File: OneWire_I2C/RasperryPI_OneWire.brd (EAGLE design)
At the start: 63.5 x 28.6 mm, 25 parts, among them U1 P82B715D, U2 DS2482-800

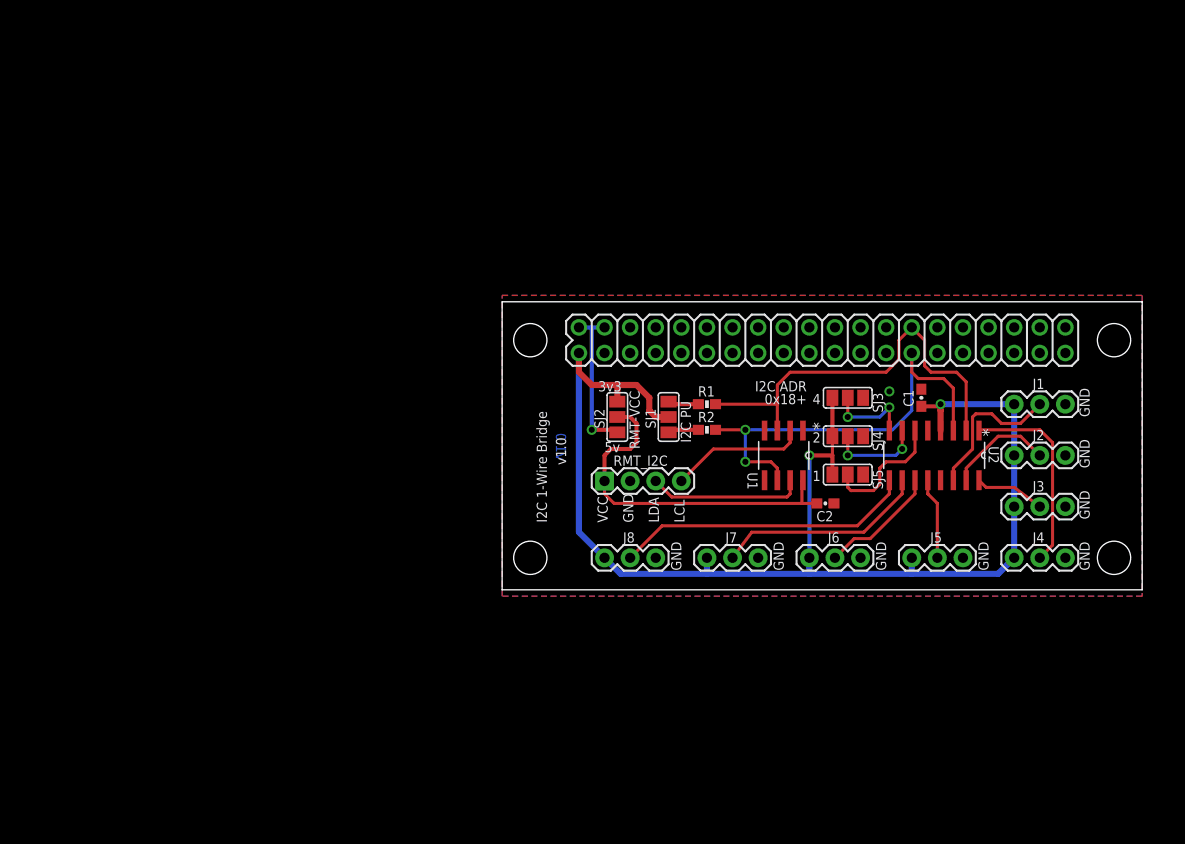
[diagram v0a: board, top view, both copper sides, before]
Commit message: Added Raspberry pi board, updated I2C extender pullup resistors to other boards
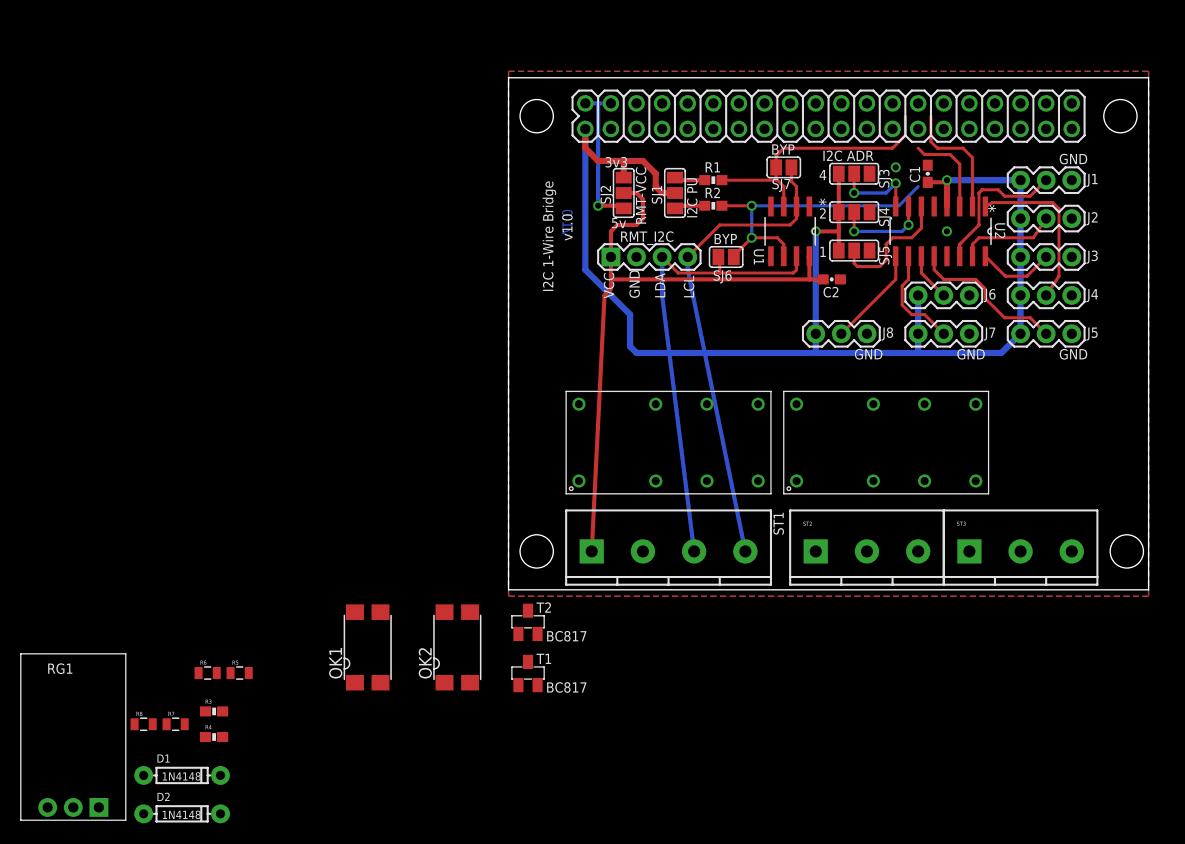
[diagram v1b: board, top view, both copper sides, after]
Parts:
- added D1, D2: 1N4148, SparkFun-DiscreteSemi:DIODE-1N4148
- added OK1, OK2: LTV816S, optocoupler:SMD4
- added R3, R4: (no value), SparkFun-Resistors:0603-RES
- added R5, R6, R7, R8: (no value), SparkFun-Resistors:0805
- added RG1: (no value), Puffin:MURATA_REG_HOR
- added RLY1, RLY2: HK19F_5V_DPDT_RELAY, Puffin:DIP16-RELAY
- added SJ6, SJ7: (no value), jumper:SJ
- added ST1: (no value), Puffin:SCREWTERM_0.2X4
- added ST2, ST3: (no value), Puffin:SCREWTERM_0.2X3
- added T1, T2: BC817, Puffin:SOT-23
- moved J7 30.5 mm to (41.3, 25.4)
- moved J8 30.5 mm to (31.1, 25.4)
- moved J6 28.2 mm to (41.3, 29.2)
- moved J4 26.0 mm to (51.4, 29.2)
- moved J3 24.8 mm to (51.4, 33.0)
- moved J5 24.7 mm to (51.4, 25.4)
- moved J2 23.5 mm to (51.4, 36.8)
- moved C2 22.2 mm to (32.7, 30.8)
- moved J1 22.2 mm to (51.4, 40.6)
- moved PI 22.2 mm to (32.4, 47.0)
- moved R1 22.2 mm to (21.0, 40.6)
- moved R2 22.2 mm to (21.0, 38.1)
- moved RMT_I2C 22.2 mm to (10.8, 33.0)
- moved SJ4 22.2 mm to (34.9, 37.5)
- moved SJ5 22.2 mm to (34.9, 33.7)
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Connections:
- new net 12V: D1.C, D2.C, OK1.4, OK2.4, RG1.1, RLY1.1, RLY2.1
- new net N$12: R4.2, T2.1
- new net N$13: D2.A, RLY2.16, T2.3
- new net N$14: D1.A, RLY1.16, T1.3
- new net N$15: R3.2, T1.1
- new net N$16: OK1.3, R3.1
- new net N$17: RLY2.4, ST3.1
- new net N$18: RLY2.6, ST3.2
- new net N$19: RLY2.8, ST3.3
- new net N$20: RLY1.4, ST2.1
- new net N$21: RLY1.6, ST2.2
- new net N$22: RLY1.8, ST2.3
- new net N$23: OK2.1, R6.1
- new net N$24: OK1.1, R5.1
- new net RLY1: OK1.2, PI.37
- new net RLY2: OK2.2, PI.35
- new net VSEL: C2.1, R7.2, R8.2, RMT_I2C.1, SJ2.2, ST1.1, U1.8
- net 3.3V: now also R5.2, R6.2
- net 5V: now also RG1.3
- net GND: now also PI.14, PI.20, RG1.2, ST1.2, T1.2, T2.2
- net LCL: now also R8.1, SJ7.1, ST1.4
- net LDA: now also R7.1, SJ6.1, ST1.3
- net N$11: now also OK2.3, R4.1; no longer C2.1, RMT_I2C.1, SJ2.2, U1.8
- net SCL: now also PI.5, SJ7.2; no longer PI.28
- net SDA: now also PI.3, SJ6.2; no longer PI.27
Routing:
- net VSEL: track 0.00 -> 64.5 mm
- net N$11: track 35.4 -> 0.00 mm
- net LCL: track 13.6 -> 47.5 mm
- net LDA: track 15.5 -> 46.6 mm
- net N$10: track 29.7 -> 9.93 mm
- net N$7: track 21.0 -> 10.4 mm
- net N$5: track 8.09 -> 15.6 mm
- net N$6: track 11.9 -> 4.81 mm
- net SDA: track 44.7 -> 39.7 mm
- net N$4: track 19.8 -> 16.6 mm
- net SCL: track 41.4 -> 38.6 mm
- net 3.3V: track 130.5 -> 133.2 mm
- net N$2: track 10.6 -> 9.78 mm
- net N$3: track 6.96 -> 7.64 mm
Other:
- board size 63.5 x 28.6 mm -> 63.5 x 50.8 mm
- board text added: "BYP"
- board text removed: "0x18+"

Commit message: Finished RPI 1Wire board
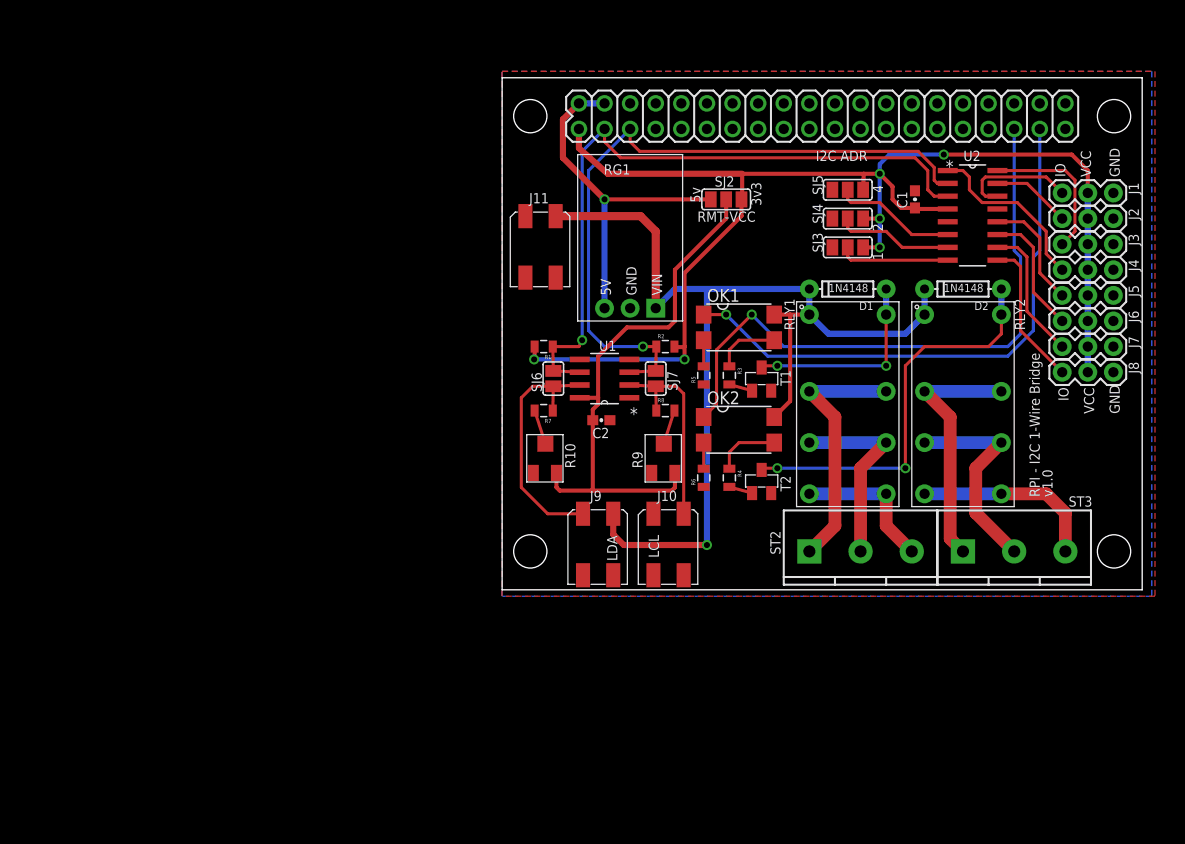
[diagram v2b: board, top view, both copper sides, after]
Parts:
- removed RMT_I2C: (no value), SparkFun-Connectors:1X04
- removed SJ1: (no value), jumper:SJ_2
- removed ST1: (no value), Puffin:SCREWTERM_0.2X4
- added J10, J11, J9: MOLEX_MINILITE_TRAP_2, Puffin:MOLEX_MINILITE_TRAP_2
- added R10, R9: (no value), Puffin:POT_3MM
- R1, R2: value 2.2k -> (none); device SparkFun-Resistors:0603-RES -> SparkFun-Resistors:0805
- R3, R4: device SparkFun-Resistors:0603-RES -> SparkFun-Resistors:0805
- moved D2 93.3 mm to (45.7, 29.8), turned to 180 degrees
- moved D1 81.8 mm to (34.3, 29.8), turned to 180 degrees
- moved RG1 74.2 mm to (12.7, 27.9)
- moved R3 61.0 mm to (22.5, 21.3), turned to 270 degrees
- moved R8 60.4 mm to (16.2, 17.8)
- moved R4 57.2 mm to (22.5, 11.1), turned to 270 degrees
- moved R5 54.7 mm to (20.0, 21.3), turned to 90 degrees
- moved R6 52.9 mm to (20.0, 11.1), turned to 90 degrees
- moved OK1 48.6 mm to (23.5, 26.0), turned to 270 degrees
- moved R7 48.0 mm to (4.13, 17.8), turned to 180 degrees
- moved T1 37.3 mm to (25.7, 21.0)
- moved OK2 35.3 mm to (23.5, 15.9), turned to 270 degrees
- moved T2 27.1 mm to (25.7, 10.8)
- moved C2 26.8 mm to (9.84, 16.8)
- moved J8 24.7 mm to (55.6, 21.6)
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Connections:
- removed net N$8: R2.1, SJ1.1
- removed net N$9: R1.1, SJ1.3
- new net N$25: R10.2, R7.2
- new net N$26: R8.2, R9.2
- net 12V: now also J11.1, J9.1
- net 3.3V: now also J1.2, J2.2, J3.2, J4.2, J5.2, J6.2, J7.2, J8.2, R1.2, R2.2; no longer J1.1, J2.1, J3.1, J4.1, J5.1, J6.1, J7.1, J8.1, R5.2, R6.2, SJ1.2
- net GND: now also J10.2, J11.2, R5.1, R6.1; no longer RMT_I2C.2, ST1.2
- net LCL: now also J10.1; no longer RMT_I2C.4, ST1.4
- net LDA: now also J9.2; no longer RMT_I2C.3, ST1.3
- net N$1: now also J1.1; no longer J1.2
- net N$10: now also J8.1; no longer J8.2
- net N$17: now also RLY2.13
- net N$18: now also RLY2.11
- net N$19: now also RLY2.9
- net N$2: now also J2.1; no longer J2.2
- net N$20: now also RLY1.13
- net N$21: now also RLY1.11
- net N$22: now also RLY1.9
- net N$23: now also OK1.2, R5.2; no longer OK2.1, R6.1
- net N$24: now also OK2.2, R6.2; no longer OK1.1, R5.1
- net N$3: now also J3.1; no longer J3.2
- net N$4: now also J4.1; no longer J4.2
- net N$5: now also J5.1; no longer J5.2
- net N$6: now also J6.1; no longer J6.2
- net N$7: now also J7.1; no longer J7.2
- net RLY1: now also OK1.1; no longer OK1.2
- net RLY2: now also OK2.1; no longer OK2.2
- net SCL: now also R2.1; no longer R1.2
- net SDA: now also R1.1; no longer R2.2
- net VSEL: now also R10.1, R9.1; no longer R7.2, R8.2, RMT_I2C.1, ST1.1
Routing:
- net 12V: track 0.00 -> 103.8 mm, vias 0 -> 1
- net RLY2: track 0.00 -> 61.2 mm, vias 0 -> 1
- net RLY1: track 0.00 -> 55.7 mm, vias 0 -> 1
- net N$13: track 0.00 -> 39.8 mm, vias 0 -> 2
- net SCL: track 38.6 -> 69.4 mm, vias 0 -> 1
- net SDA: track 39.7 -> 68.9 mm, vias 2 -> 1
- net LCL: track 47.5 -> 20.0 mm
- net N$20: track 0.00 -> 25.6 mm
- net N$17: track 0.00 -> 25.1 mm
- net LDA: track 46.6 -> 24.8 mm
- net N$18: track 0.00 -> 21.0 mm
- net 5V: track 15.3 -> 35.8 mm
- net N$14: track 0.00 -> 20.0 mm, vias 0 -> 2
- net N$21: track 0.00 -> 19.5 mm
- net N$19: track 0.00 -> 18.6 mm
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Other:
- board text added: "5V"
- board text added: "IO"
- board text added: "RPI - I2C 1-Wire Bridge"
- board text added: "VIN"
- board text removed: "BYP"
- board text removed: "I2C 1-Wire Bridge"
- board text removed: "I2C PU"

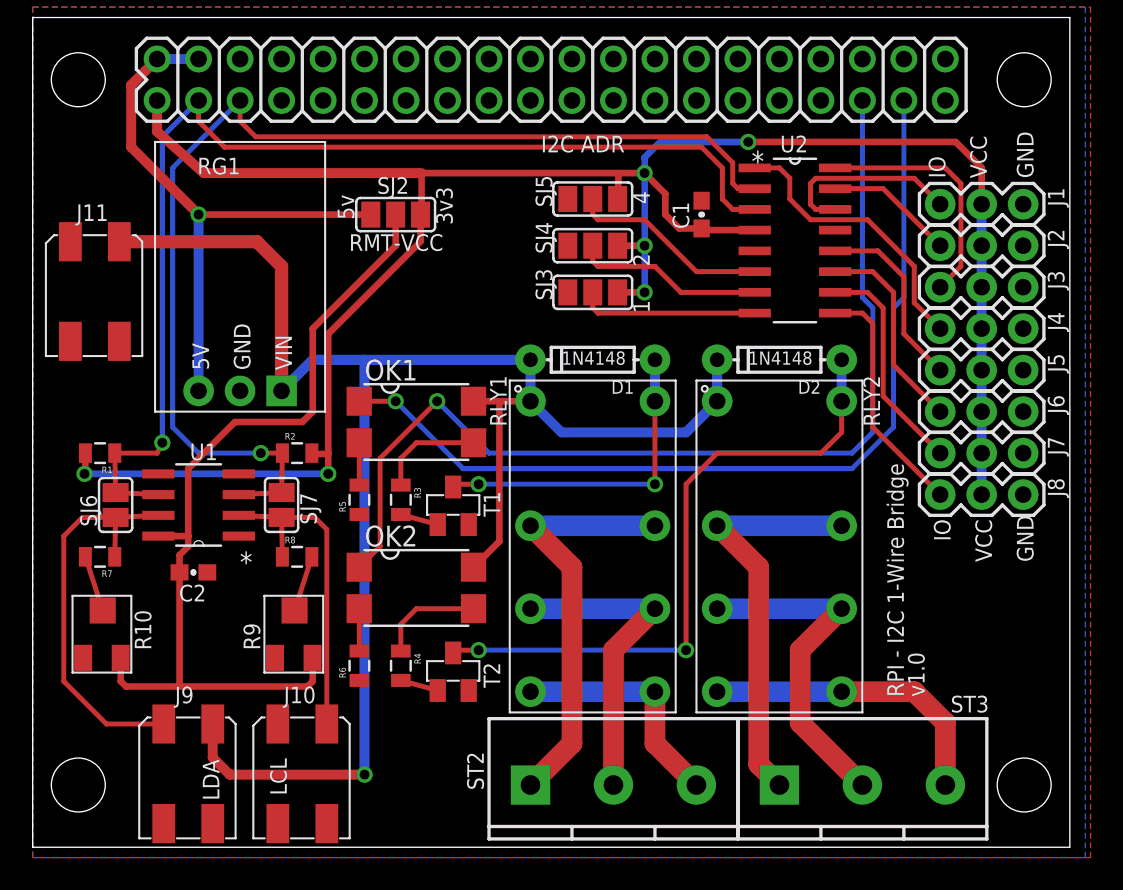
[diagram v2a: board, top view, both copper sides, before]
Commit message: Standardized i2c connections, fixed 1Wire connections, lots of cleanup
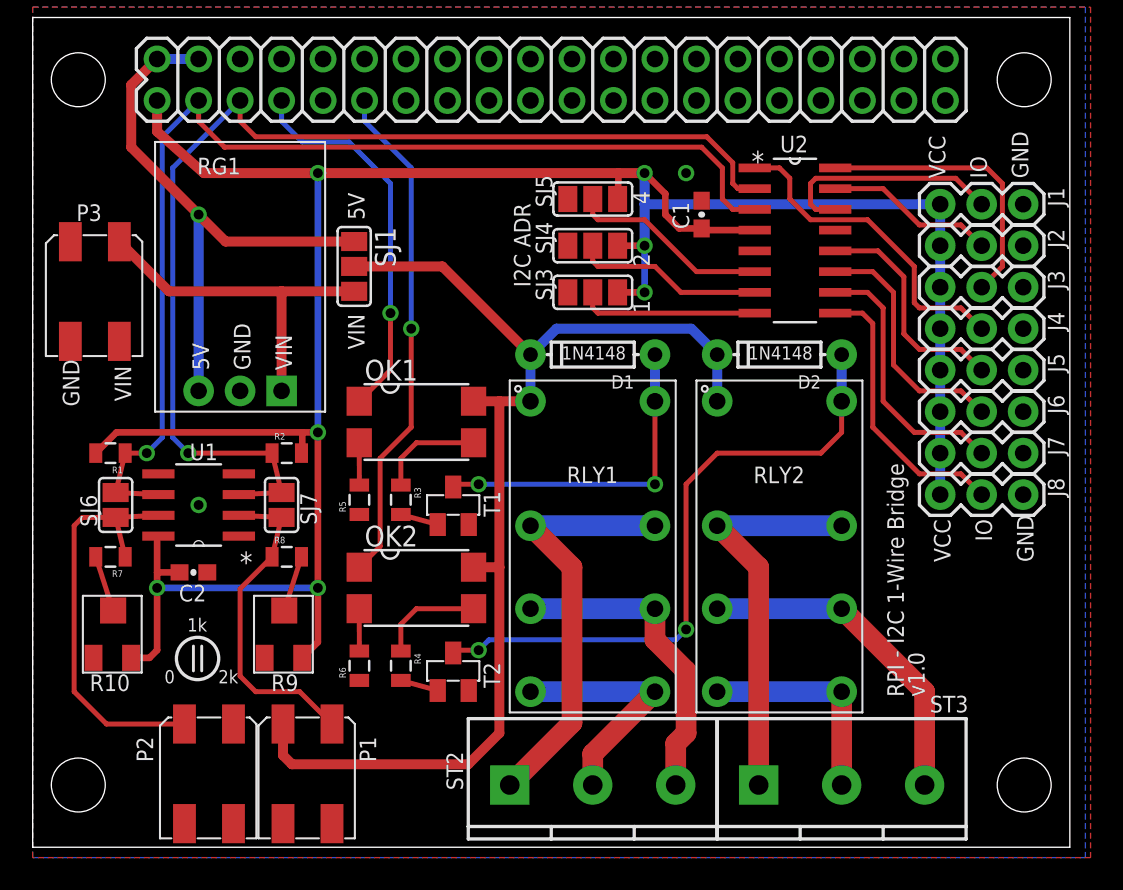
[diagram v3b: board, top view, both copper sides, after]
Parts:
- removed J10, J9: MOLEX_MINILITE_TRAP_2, Puffin:MOLEX_MINILITE_TRAP_2
- removed SJ2: (no value), jumper:SJ_2
- added P1, P2: MOLEX_MINILITE_TRAP_2, Puffin:MOLEX_MINILITE_TRAP_2
- added SJ1: (no value), jumper:SJ_2
- moved ST2 1.27 mm to (29.2, 3.81)
- moved ST3 1.27 mm to (44.5, 3.81)
- moved R1 0.63 mm to (4.76, 24.1)
- moved R10 0.63 mm to (3.17, 10.8)
- moved R2 0.63 mm to (15.6, 24.1)
- moved R7 0.63 mm to (4.76, 17.8)
- moved R8 0.63 mm to (15.6, 17.8)
- moved R9 0.63 mm to (13.7, 10.8)
- moved D1 0.32 mm to (34.3, 30.2)
- moved D2 0.32 mm to (45.7, 30.2)
- renumbered J11 to P3
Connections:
- removed net VSEL: C2.1, R10.1, R9.1, SJ2.2, U1.8
- new net VCC: D1.C, D2.C, OK1.4, OK2.4, P1.2, RLY1.1, RLY2.1, SJ1.2
- net 12V: now also SJ1.3; no longer D1.C, D2.C, J9.1, OK1.4, OK2.4, RLY1.1, RLY2.1
- net 3.3V: now also C2.1, J1.1, J2.1, J3.1, J4.1, J5.1, J6.1, J7.1, J8.1, R10.1, R9.1, U1.8; no longer J1.2, J2.2, J3.2, J4.2, J5.2, J6.2, J7.2, J8.2, SJ2.3
- net 5V: now also SJ1.1; no longer SJ2.1
- net GND: now also P2.1; no longer J10.2
- net LCL: now also P1.1; no longer J10.1
- net LDA: now also P2.2; no longer J9.2
- net N$1: now also J1.2; no longer J1.1
- net N$10: now also J8.2; no longer J8.1
- net N$18: now also ST3.3; no longer ST3.2
- net N$19: now also ST3.2; no longer ST3.3
- net N$2: now also J2.2; no longer J2.1
- net N$21: now also ST2.3; no longer ST2.2
- net N$22: now also ST2.2; no longer ST2.3
- net N$3: now also J3.2; no longer J3.1
- net N$4: now also J4.2; no longer J4.1
- net N$5: now also J5.2; no longer J5.1
- net N$6: now also J6.2; no longer J6.1
- net N$7: now also J7.2; no longer J7.1
- net RLY1: now also PI.7; no longer PI.37
- net RLY2: now also PI.11; no longer PI.35
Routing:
- net 12V: track 103.8 -> 21.7 mm, vias 1 -> 0
- net VCC: track 0.00 -> 73.4 mm
- net VSEL: track 53.5 -> 0.00 mm
- net RLY1: track 55.7 -> 23.6 mm
- net RLY2: track 61.2 -> 31.1 mm
- net 3.3V: track 134.6 -> 155.2 mm, vias 6 -> 7
- net N$19: track 18.6 -> 13.3 mm
- net N$7: track 13.7 -> 16.4 mm
- net N$5: track 11.5 -> 14.0 mm
- net N$2: track 7.87 -> 10.4 mm
- net N$6: track 12.6 -> 15.1 mm
- net N$4: track 17.5 -> 20.0 mm
- net N$10: track 14.7 -> 17.3 mm
- net N$3: track 15.0 -> 17.5 mm
- net N$1: track 11.6 -> 14.2 mm
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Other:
- board text added: "0"
- board text added: "1k"
- board text added: "2k"
- board text added: "C"
- board text added: "NC"
- board text added: "NO"
- board text added: "SCL"
- board text added: "SDA"
- board text added: "VOUT"
- board text removed: "3v3"
- board text removed: "5v"
- board text removed: "RMT-VCC"

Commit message: Gate 4, and misc updates
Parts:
- removed ST3: (no value), Puffin:SCREWTERM_0.2X3
- removed U$1, U$2, U$3, U$4: (no value), SparkFun-Electromechanical:STAND-OFF
- added ST1: (no value), Puffin:SCREWTERM_0.2X3
- added U$6: (no value), Puffin:RPI_BOARD
- moved RG1 17.4 mm to (3.17, 42.5), turned to 270 degrees
- moved SJ1 6.70 mm to (20.3, 42.2)
- moved PI 5.55 mm to (32.5, 52.5)
- moved J1 5.54 mm to (56.8, 44.8)
- moved J2 5.54 mm to (56.8, 42.2)
- moved J3 5.54 mm to (56.8, 39.7)
- moved J4 5.54 mm to (56.8, 37.1)
- moved J5 5.54 mm to (56.8, 34.6)
- moved J6 5.54 mm to (56.8, 32.1)
- moved J7 5.54 mm to (56.8, 29.5)
- moved J8 5.54 mm to (56.8, 27.0)
- moved C1 5.43 mm to (41.6, 44.1)
- moved SJ3 5.43 mm to (34.9, 39.4)
- moved SJ4 5.43 mm to (34.9, 42.2)
- moved SJ5 5.43 mm to (34.9, 45.1)
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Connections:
- net N$17: now also ST1.1; no longer ST3.1
- net N$18: now also ST1.3; no longer ST3.3
- net N$19: now also ST1.2; no longer ST3.2
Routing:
- net SDA: track 68.0 -> 74.4 mm
- net 12V: track 21.7 -> 27.7 mm
- net 5V: track 35.4 -> 29.6 mm, vias 1 -> 0
- net 3.3V: track 155.2 -> 160.9 mm
- net VCC: track 73.4 -> 78.6 mm
- net RLY1: track 23.6 -> 27.5 mm
- net RLY2: track 31.1 -> 34.9 mm
- net SCL: track 69.2 -> 71.0 mm
- net N$13: track 39.3 -> 40.8 mm
- net N$20: track 26.1 -> 27.4 mm
- net N$21: track 19.5 -> 20.7 mm
- net N$19: track 13.3 -> 14.6 mm
- net N$18: track 20.5 -> 21.8 mm
- net N$17: track 24.5 -> 25.8 mm
- net N$22: track 14.9 -> 16.1 mm
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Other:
- board size 63.5 x 50.8 mm -> 65.1 x 56 mm
